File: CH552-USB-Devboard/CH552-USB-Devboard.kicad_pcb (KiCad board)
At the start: 2 copper layers, 23 parts, among them J1 Conn_01x10_Male, J2 Conn_01x10_Male, J3 USB_A, SW1 SW_Push, SW2 SW_Push, U1 CH552T, U2 CH552G, Y1 Crystal

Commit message: started on layout
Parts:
- C5, C6, U2, Y1: moved to B.Cu
- J3: value USB_A -> USB_B_Micro; footprint Connector_USB:USB_A_CNCTech_1001-011-01101_Horizontal -> digikey-footprints:USB_Micro_B_Female_10118193-0001LF
- SW1, SW2: footprint Button_Switch_SMD:SW_DIP_SPSTx01_Slide_6.7x4.1mm_W6.73mm_P2.54mm_LowProfile_JPin -> Button_Switch_SMD:SW_SPST_PTS810
- moved SW1 84.6 mm to (77.5, 105.9)
- moved R1 84.1 mm to (81.1, 98.8)
- moved C4 72.3 mm to (80.7, 87.4)
- moved D2 71.3 mm to (81.5, 94.4)
- moved R4 71.2 mm to (85.5, 94.6), turned to 180 degrees
- moved C3 67.6 mm to (81.3, 89.4)
- moved R5 66.9 mm to (85.5, 96.2)
- moved R2 64.0 mm to (85.5, 87.4)
- moved D3 62.8 mm to (81.5, 96.4)
- moved C2 57.5 mm to (81.9, 75.0)
- moved C1 56.0 mm to (81.9, 76.6)
- moved SW2 53.6 mm to (89.9, 106.2)
- moved R3 42.5 mm to (85.4, 92.4)
- moved JP1 40.0 mm to (86.0, 98.4)
- moved D1 34.9 mm to (81.5, 92.5)
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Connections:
- J3 pad 4: GND -> Net-(J3-Pad4)

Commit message: more schmatic work multilanding
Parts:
- U2: moved to F.Cu
- moved C1 65.9 mm to (147.9, 75.7)
- moved C2 65.9 mm to (147.9, 74.1)
- moved C3 54.0 mm to (135.2, 90.8)
- moved D2 54.0 mm to (135.4, 95.8)
- moved D3 54.0 mm to (135.4, 97.8)
- moved JP1 54.0 mm to (139.9, 99.8)
- moved R1 54.0 mm to (135.1, 100.2)
- moved R2 54.0 mm to (139.4, 88.8)
- moved R3 54.0 mm to (139.3, 93.8)
- moved R4 54.0 mm to (139.4, 96.0)
- moved R5 54.0 mm to (139.5, 97.6)
- moved C4 54.0 mm to (134.6, 88.8)
- moved D1 54.0 mm to (135.5, 93.9)
- moved SW1 31.1 mm to (105.9, 93.2)
- moved SW2 24.0 mm to (106.0, 88.3)
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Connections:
- U1 pad 10: /P3.3 -> /P3.0
- U1 pad 11: (no net) -> /P3.3
- U2 pad 15: +3V3 -> VCC
- U2 pad 16: VCC -> +3V3
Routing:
- net /P3.7: track 0.00 -> 39.0 mm, vias 0 -> 1
- net /P3.6: track 0.00 -> 34.5 mm, vias 0 -> 1
- net /P3.5: track 0.00 -> 27.0 mm, vias 0 -> 1
- net /P3.4: track 0.00 -> 26.6 mm, vias 0 -> 1
- net /P3.3: track 0.00 -> 22.2 mm, vias 0 -> 1
- net /P1.7: track 0.00 -> 22.1 mm
- net /P1.3: track 0.00 -> 20.5 mm, vias 0 -> 1
- net /P3.2: track 0.00 -> 19.6 mm, vias 0 -> 1
- net /P1.6: track 0.00 -> 18.7 mm
- net /P1.5: track 0.00 -> 15.7 mm
- net /P1.4: track 0.00 -> 14.0 mm
- net /P3.0: track 0.00 -> 12.3 mm, vias 0 -> 2
- net /P1.0: track 0.00 -> 11.6 mm, vias 0 -> 1
- net /P3.1: track 0.00 -> 10.6 mm, vias 0 -> 1
- net /P1.1: track 0.00 -> 4.87 mm
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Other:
- net class Default: trace_width 0.25 -> 0.2

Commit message: first route done
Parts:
- moved C2 67.9 mm to (80.0, 73.7), turned to 90 degrees
- moved R5 67.0 mm to (77.3, 72.8)
- moved C1 65.9 mm to (82.0, 73.6), turned to 90 degrees
- moved D3 64.3 mm to (77.3, 70.4), turned to 180 degrees
- moved R3 60.4 mm to (79.2, 99.0), turned to 90 degrees
- moved R2 58.3 mm to (81.2, 90.9), turned to 270 degrees
- moved C3 55.7 mm to (79.6, 92.7), turned to 90 degrees
- moved JP1 54.9 mm to (85.1, 100.2), turned to 180 degrees
- moved D1 54.7 mm to (81.0, 99.0), turned to 90 degrees
- moved R1 54.2 mm to (81.2, 94.3), turned to 90 degrees
- moved R4 48.3 mm to (91.2, 98.9), turned to 90 degrees
- moved D2 46.2 mm to (89.4, 99.1), turned to 90 degrees
- moved C4 45.9 mm to (92.3, 71.0)
- moved C5 26.6 mm to (88.8, 91.3), turned to 90 degrees
- moved Y1 25.6 mm to (85.0, 94.7), turned to 270 degrees
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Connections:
- R3 pad 1: Net-(R3-Pad1) -> VCC
- R4 pad 1: Net-(R4-Pad1) -> VCC
- R5 pad 1: Net-(R3-Pad1) -> VCC
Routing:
- net VCC: track 3.62 -> 85.1 mm, vias 0 -> 5
- net /P1.2: track 0.00 -> 34.7 mm, vias 0 -> 3
- net /RESET: track 3.76 -> 31.6 mm, vias 0 -> 1
- net /P1.3: track 20.5 -> 44.9 mm, vias 1 -> 2
- net /P3.0: track 12.3 -> 31.7 mm
- net /P1.1: track 4.87 -> 22.3 mm, vias 0 -> 1
- net /P3.1: track 10.6 -> 27.0 mm
- net /P3.6: track 34.5 -> 50.5 mm, vias 1 -> 4
- net /P1.5: track 15.7 -> 26.0 mm, vias 0 -> 1
- net Net-(JP1-Pad2): track 0.00 -> 9.41 mm
- net +3V3: track 4.35 -> 13.0 mm, vias 0 -> 2
- net Net-(R1-Pad1): track 0.00 -> 6.28 mm
- net /P3.7: track 39.0 -> 43.9 mm, vias 1 -> 2
- net Net-(D3-Pad2): track 0.00 -> 3.21 mm
- net Net-(D1-Pad2): track 0.00 -> 1.89 mm
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
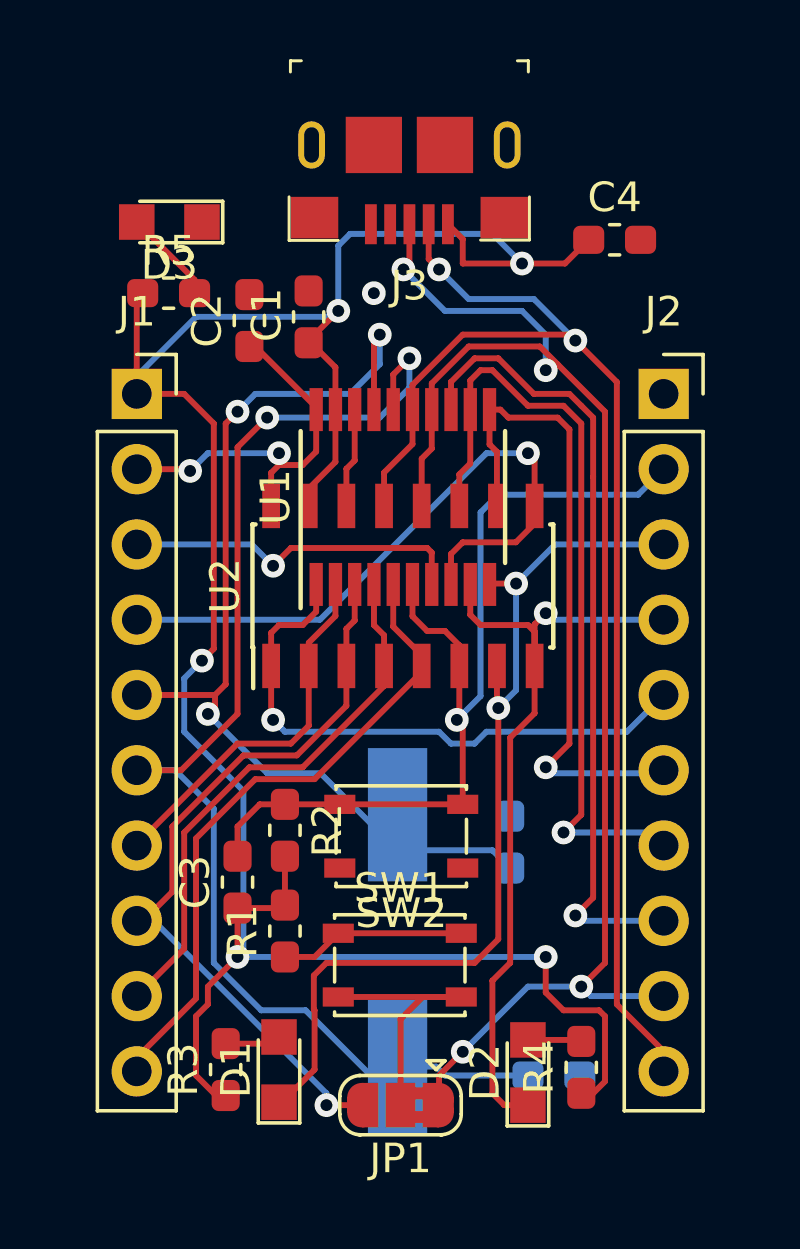
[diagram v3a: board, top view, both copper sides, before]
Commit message: ROUTING COMPLETE AND DRC DONE READY FOR SILK
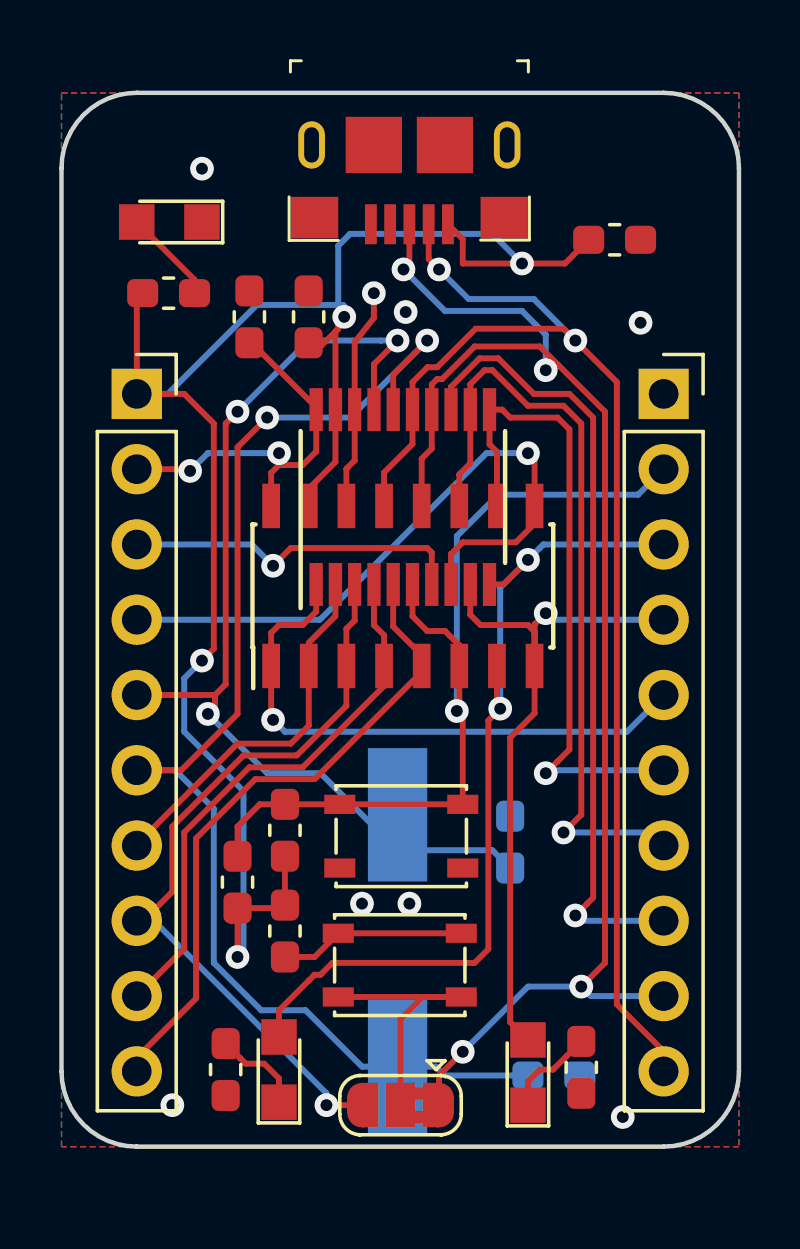
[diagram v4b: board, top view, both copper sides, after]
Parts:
- moved C2 0.12 mm to (80.0, 73.6)
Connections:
- D1 pad 1: /P3.0 -> Net-(D1-Pad1)
- D1 pad 2: Net-(D1-Pad2) -> /P3.0
- D2 pad 1: /P3.1 -> Net-(D2-Pad1)
- D2 pad 2: Net-(D2-Pad2) -> /P3.1
- J3 pad SH: (no net) -> GND
- R3 pad 1: VCC -> GND
- R3 pad 2: Net-(D1-Pad2) -> Net-(D1-Pad1)
- R4 pad 1: VCC -> GND
- R4 pad 2: Net-(D2-Pad2) -> Net-(D2-Pad1)
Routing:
- net VCC: track 85.1 -> 62.6 mm, vias 5 -> 4
- net GND: track 3.37 -> 7.52 mm, vias 1 -> 8
- net /P3.1: track 27.0 -> 23.4 mm
- net Net-(D1-Pad1): track 0.00 -> 3.19 mm
- net Net-(D2-Pad1): track 0.00 -> 3.16 mm
- net Net-(D1-Pad2): track 1.89 -> 0.00 mm
- net Net-(D2-Pad2): track 1.82 -> 0.00 mm
- net /P3.0: track 31.7 -> 30.5 mm
- added copper zone on B.Cu, net GND
- added copper zone on F.Cu, net GND
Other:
- board outline added: 22.9 x 35.6 mm

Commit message: silks complete v1 ready
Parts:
- added G***: LOGO, ArtandSilks:rearsilk, B.Cu at (85.2, 85.1)
- added G***: LOGO, ArtandSilks:frontsilk, F.Cu at (85.2, 83.3)
- moved C6 1.77 mm to (88.8, 98.2), turned to 90 degrees
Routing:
- net /P1.3: track 44.4 -> 43.6 mm
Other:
- board text added: "By Rabid Inventor"
- board text added: "V1.0"

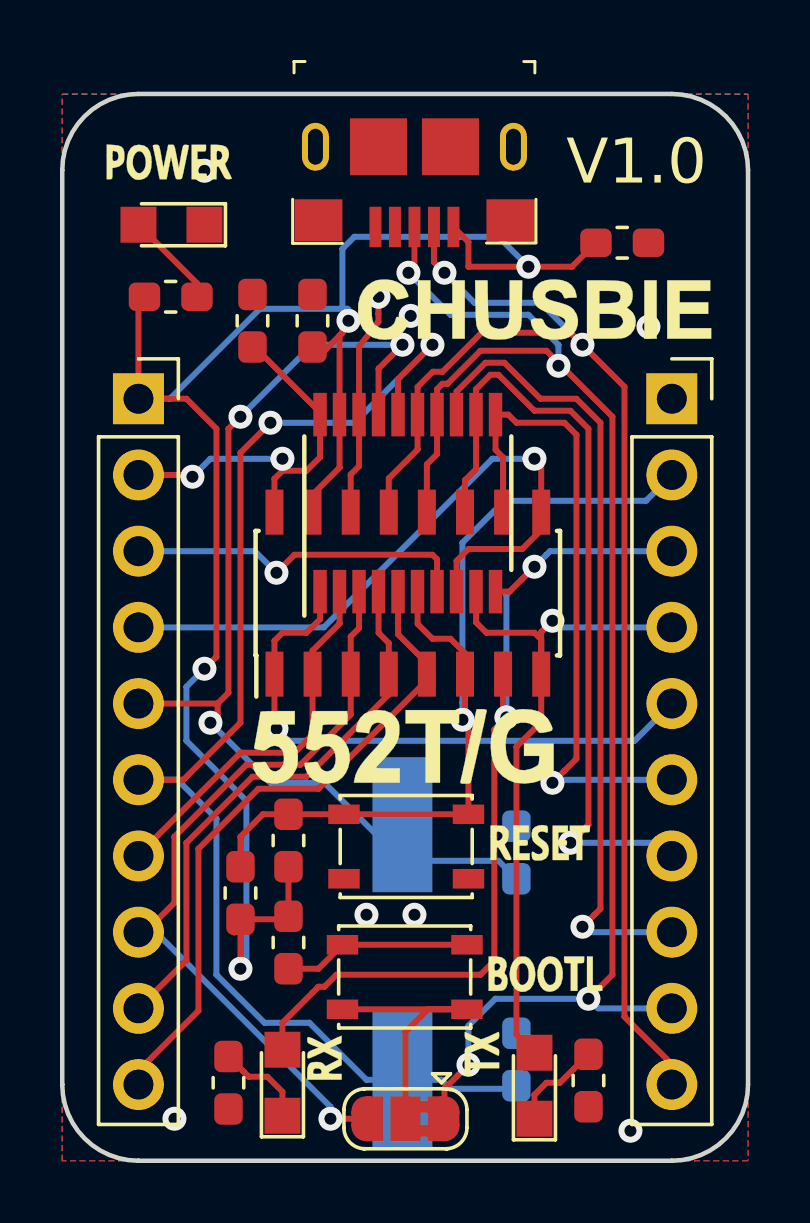
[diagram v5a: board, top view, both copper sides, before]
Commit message: tied bootloader switch to gnd not vcc and silk fixes
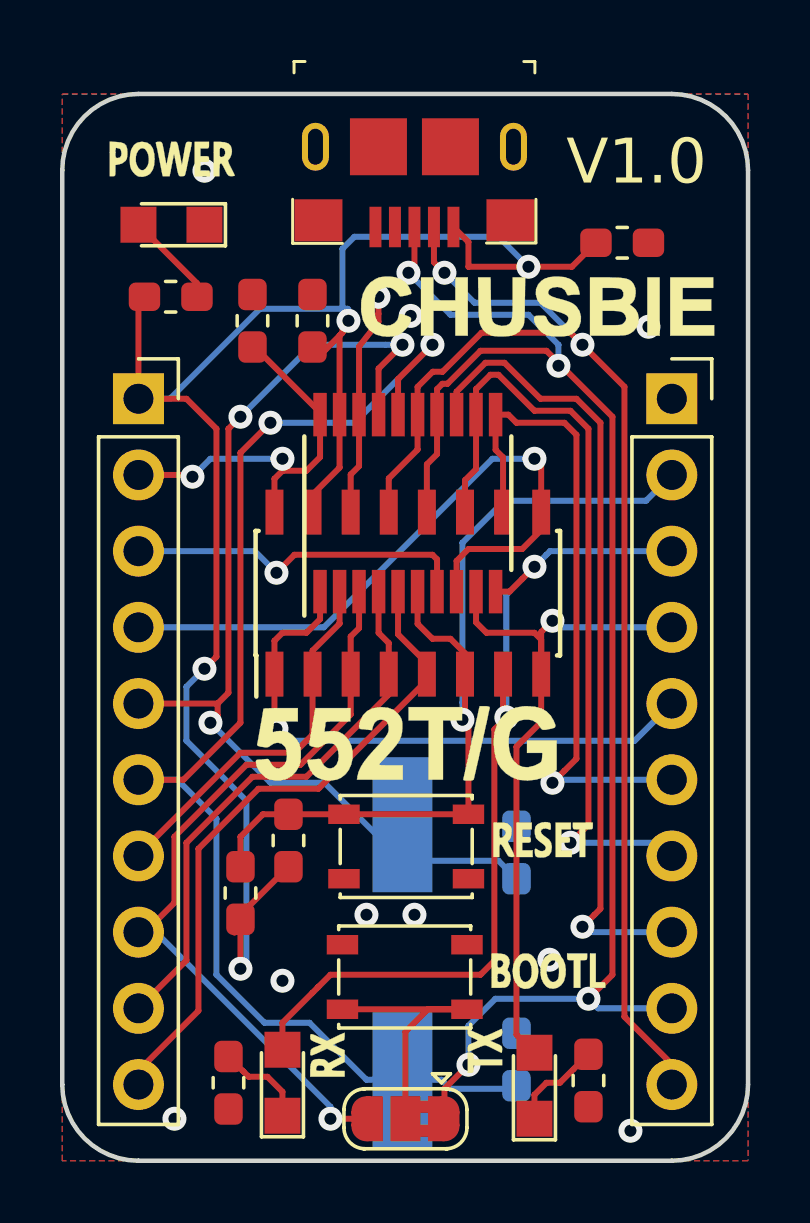
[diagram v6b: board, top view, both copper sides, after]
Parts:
- removed R1: 10k, Resistor_SMD:R_0603_1608Metric_Pad1.05x0.95mm_HandSolder
- moved G*** 0.28 mm to (85.0, 84.9)
- moved G*** 0.14 mm to (85.3, 83.2)
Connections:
- SW1 pad 1: Net-(R1-Pad1) -> GND
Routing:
- net Net-(R1-Pad1): track 6.28 -> 0.00 mm
- net VCC: track 62.6 -> 61.7 mm
- net GND: vias 8 -> 10
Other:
- board text removed: "By Rabid Inventor"

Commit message: checked and sent to porduction
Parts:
- removed JP1: SolderJumper_3_Bridged12, Jumper:SolderJumper-3_P1.3mm_Bridged2Bar12_RoundedPad1.0x1.5mm
- removed R2: 10k, Resistor_SMD:R_0603_1608Metric_Pad1.05x0.95mm_HandSolder
- moved G*** 0.41 mm to (85.4, 83.6)
- moved G*** 0.22 mm to (85.2, 85.0)
- moved D2 0.20 mm to (89.4, 98.9)
- moved SW2 0.16 mm to (85.1, 91.3), turned to 0 degrees
- moved D1 0.10 mm to (81.0, 98.9)
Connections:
- SW1 pad 1: GND -> +3V3
- SW1 pad 2: Net-(JP1-Pad2) -> /P3.6
- SW2 pad 1: GND -> /RESET
- SW2 pad 2: /RESET -> VCC
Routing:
- net +3V3: track 13.0 -> 34.2 mm, vias 2 -> 4
- net /P1.5: track 26.0 -> 15.8 mm, vias 1 -> 0
- net Net-(JP1-Pad2): track 9.41 -> 0.00 mm
- net VCC: track 61.7 -> 67.3 mm
- net /P3.6: track 50.8 -> 52.8 mm
- net /P3.0: track 30.5 -> 31.2 mm
- net /P3.3: track 22.3 -> 21.7 mm
- net GND: vias 10 -> 16

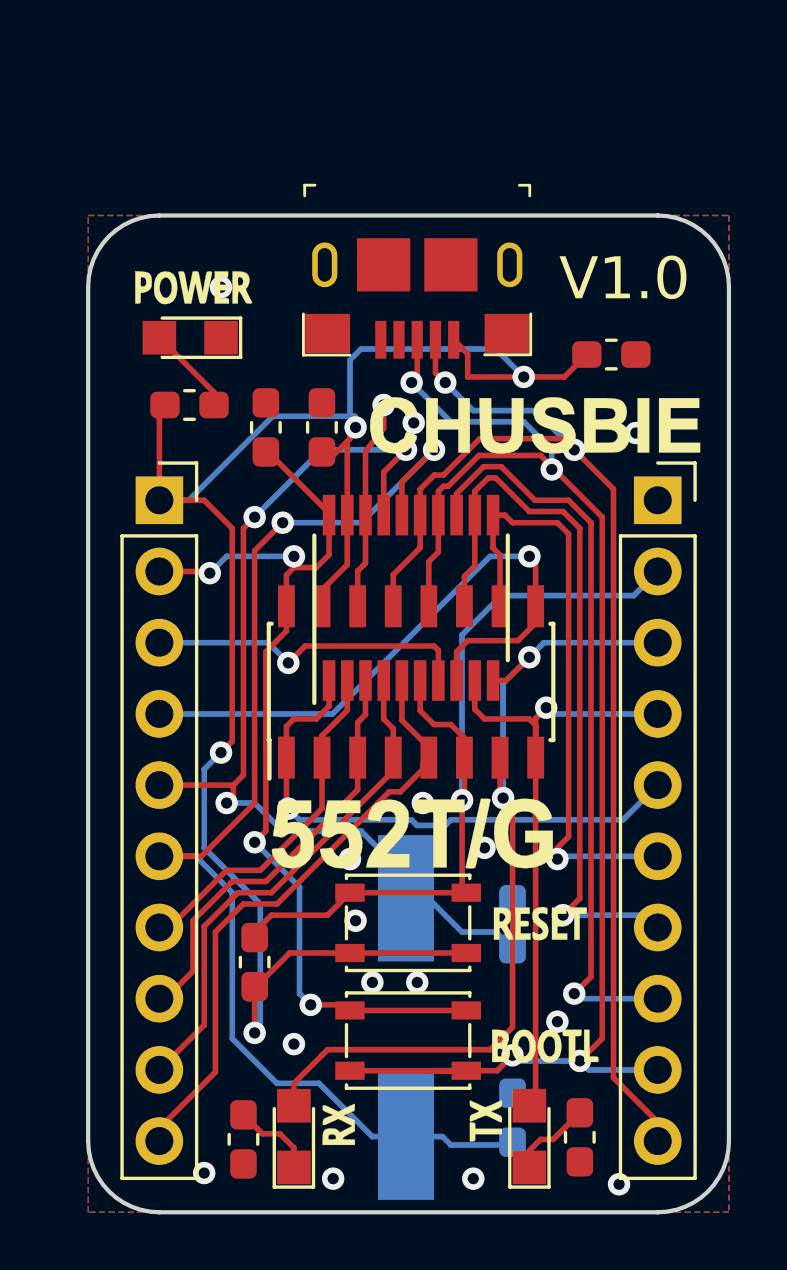
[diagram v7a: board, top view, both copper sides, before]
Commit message: routing started on v2
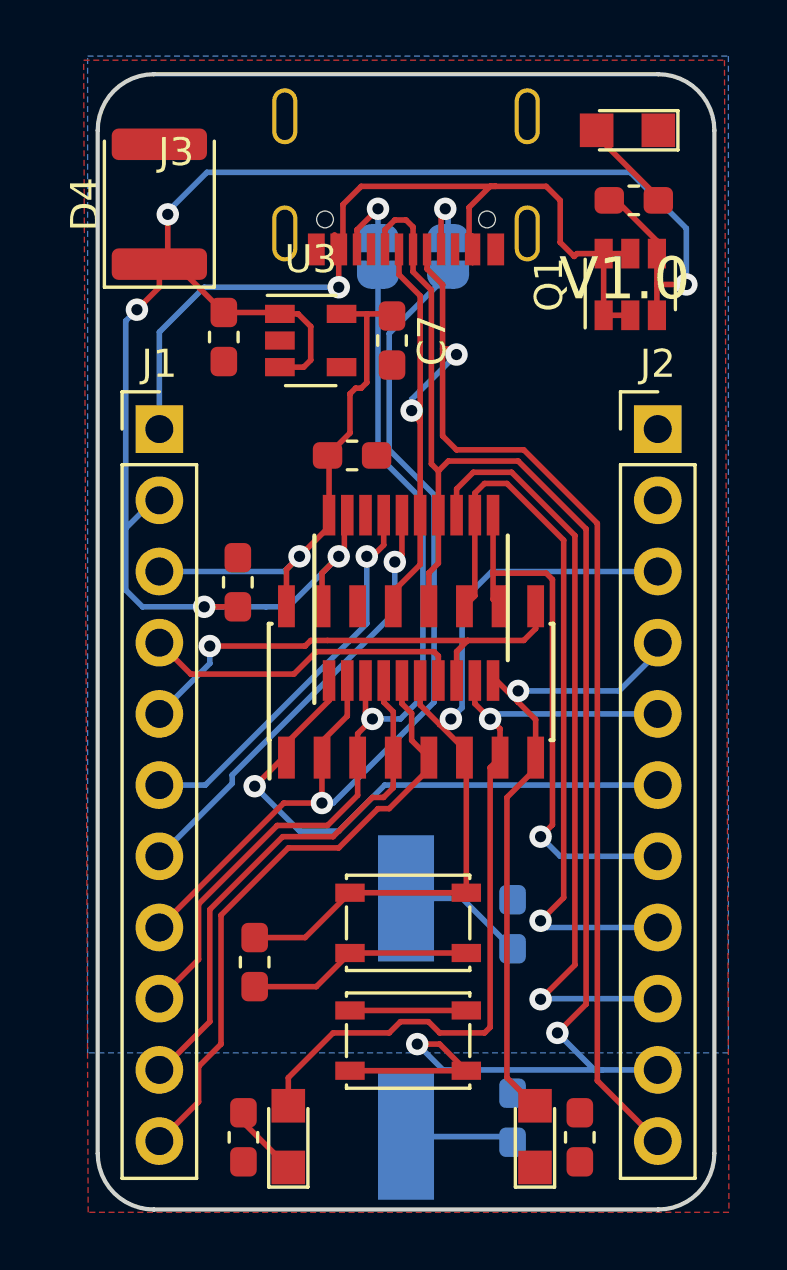
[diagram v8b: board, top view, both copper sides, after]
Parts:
- removed G***: LOGO, ArtandSilks:frontsilk
- removed G***: LOGO, ArtandSilks:rearsilk
- added C7: 1uF, Capacitor_SMD:C_0603_1608Metric_Pad1.05x0.95mm_HandSolder, F.Cu at (84.5, 70.5)
- added D4: D_ALT, Diode_SMD:D_1812_4532Metric, F.Cu at (76.2, 65.6)
- added JP1: Jumper, Jumper:SolderJumper-2_P1.3mm_Bridged_RoundedPad1.0x1.5mm, B.Cu at (86.5, 67.5)
- added JP2: Jumper, Jumper:SolderJumper-2_P1.3mm_Bridged_RoundedPad1.0x1.5mm, B.Cu at (84.0, 67.5)
- added Q1: CPH6337, TO_SOT_Packages_SMD:SOT-23-6, F.Cu at (93.0, 68.5)
- added U3: MIC5504-3.3YM5, Package_TO_SOT_SMD:SOT-23-5, F.Cu at (81.6, 70.5)
- C4: value 100nF -> 1uF
- J1, J2: value Conn_01x10_Male -> Conn_01x11_Male; footprint Connector_PinSocket_2.54mm:PinSocket_1x10_P2.54mm_Vertical -> Connector_PinHeader_2.54mm:PinHeader_1x11_P2.54mm_Vertical
- J3: value USB_B_Micro -> USB_C_Receptacle; footprint digikey-footprints:USB_Micro_B_Female_10118193-0001LF -> footprint:VACON_CSP_USC16_TR
- moved R5 17.5 mm to (93.1, 65.5)
- moved D3 17.3 mm to (92.9, 63.0)
- moved C4 13.8 mm to (78.5, 70.4), turned to 270 degrees
- moved R3 12.0 mm to (91.2, 98.9)
- moved R4 12.0 mm to (79.2, 98.9)
- moved D2 8.60 mm to (80.8, 98.9)
- moved D1 8.60 mm to (89.6, 98.9)
- moved C1 6.29 mm to (79.0, 79.1)
- moved C2 3.23 mm to (83.1, 74.6), turned to 0 degrees
- moved J1 2.54 mm to (76.2, 73.7)
- moved J2 2.54 mm to (94.0, 73.7)
- moved J3 1.19 mm to (85.0, 66.7)
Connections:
- J1 pad 1: VCC -> VBUS
- J1 pad 10: /P1.7 -> /P1.6
- J1 pad 2: +3V3 -> VCC
- J1 pad 3: /P1.0 -> +3V3
- J1 pad 4: /P1.1 -> /P1.0
- J1 pad 5: /P1.2 -> /P1.1
- J1 pad 6: /P1.3 -> /P1.2
- J1 pad 7: /P1.4 -> /P1.3
- J1 pad 8: /P1.5 -> /P1.4
- J1 pad 9: /P1.6 -> /P1.5
- J2 pad 10: /P3.7 -> /P3.6
- J2 pad 2: /RESET -> GND
- J2 pad 3: /P3.0 -> /RESET
- J2 pad 4: /P3.1 -> /P3.0
- J2 pad 5: /P3.2 -> /P3.1
- J2 pad 6: /P3.3 -> /P3.2
- J2 pad 7: /P3.4 -> /P3.3
- J2 pad 8: /P3.5 -> /P3.4
- J2 pad 9: /P3.6 -> /P3.5
- J3 pad 1: VCC -> GND
- U2 pad 7: /P3.0 -> /P3.1
- U2 pad 8: /P3.1 -> /P3.0
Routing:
- net VBUS: track 0.00 -> 32.7 mm, vias 0 -> 1
- net /P1.3: track 43.6 -> 19.6 mm, vias 2 -> 1
- net /P1.4: track 12.5 -> 34.7 mm, vias 0 -> 1
- net /P1.5: track 15.8 -> 33.5 mm, vias 0 -> 1
- net /P1.2: track 35.1 -> 18.6 mm, vias 3 -> 1
- net +3V3: track 34.2 -> 23.0 mm, vias 4 -> 1
- net /P3.7: track 44.1 -> 53.8 mm
- net /P3.0: track 31.2 -> 23.0 mm, vias 2 -> 1
- net GND: track 7.52 -> 0.00 mm, vias 16 -> 0
- net VCC: track 67.3 -> 74.0 mm, vias 4 -> 5
- net /P3.6: track 52.8 -> 58.2 mm, vias 4 -> 2
- net /P3.1: track 23.1 -> 28.2 mm
- net /P1.1: track 22.3 -> 17.4 mm
- net Net-(D1-Pad1): track 3.19 -> 0.00 mm
- net /CC2: track 0.00 -> 2.81 mm, vias 0 -> 1
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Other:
- board size 22.9 x 35.6 mm -> 22 x 40.5 mm
